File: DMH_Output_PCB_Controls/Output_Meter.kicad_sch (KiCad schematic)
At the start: 63 parts, among them Q1 BC558, Q2 BC558, U1 TL072, U2 LM339, U3 LM339, U4 LM339, U5 LM339, U6 LM339

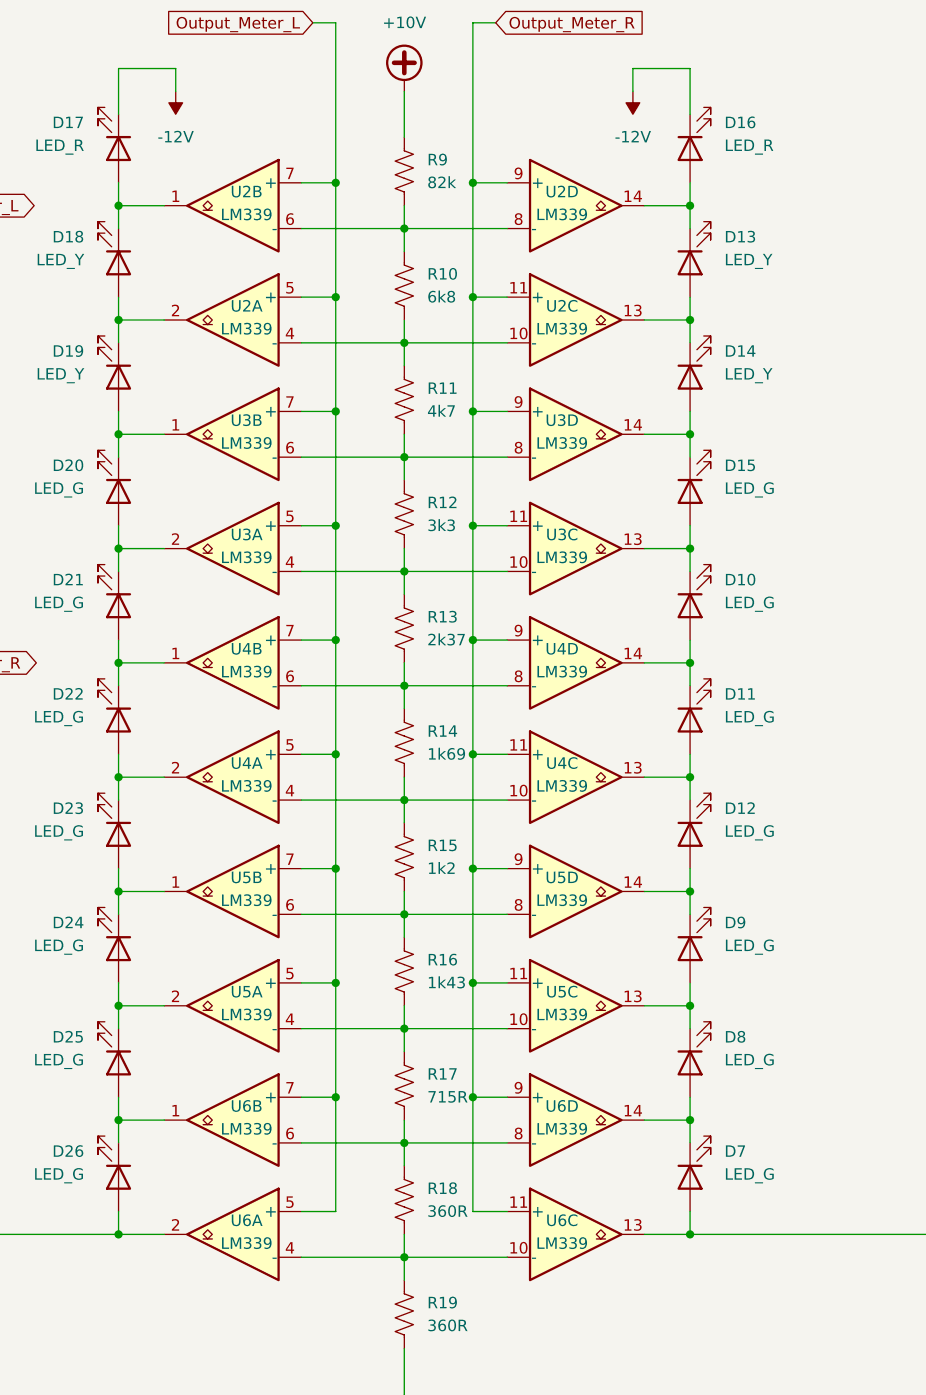
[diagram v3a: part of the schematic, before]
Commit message: Re-arranged LM339 connections
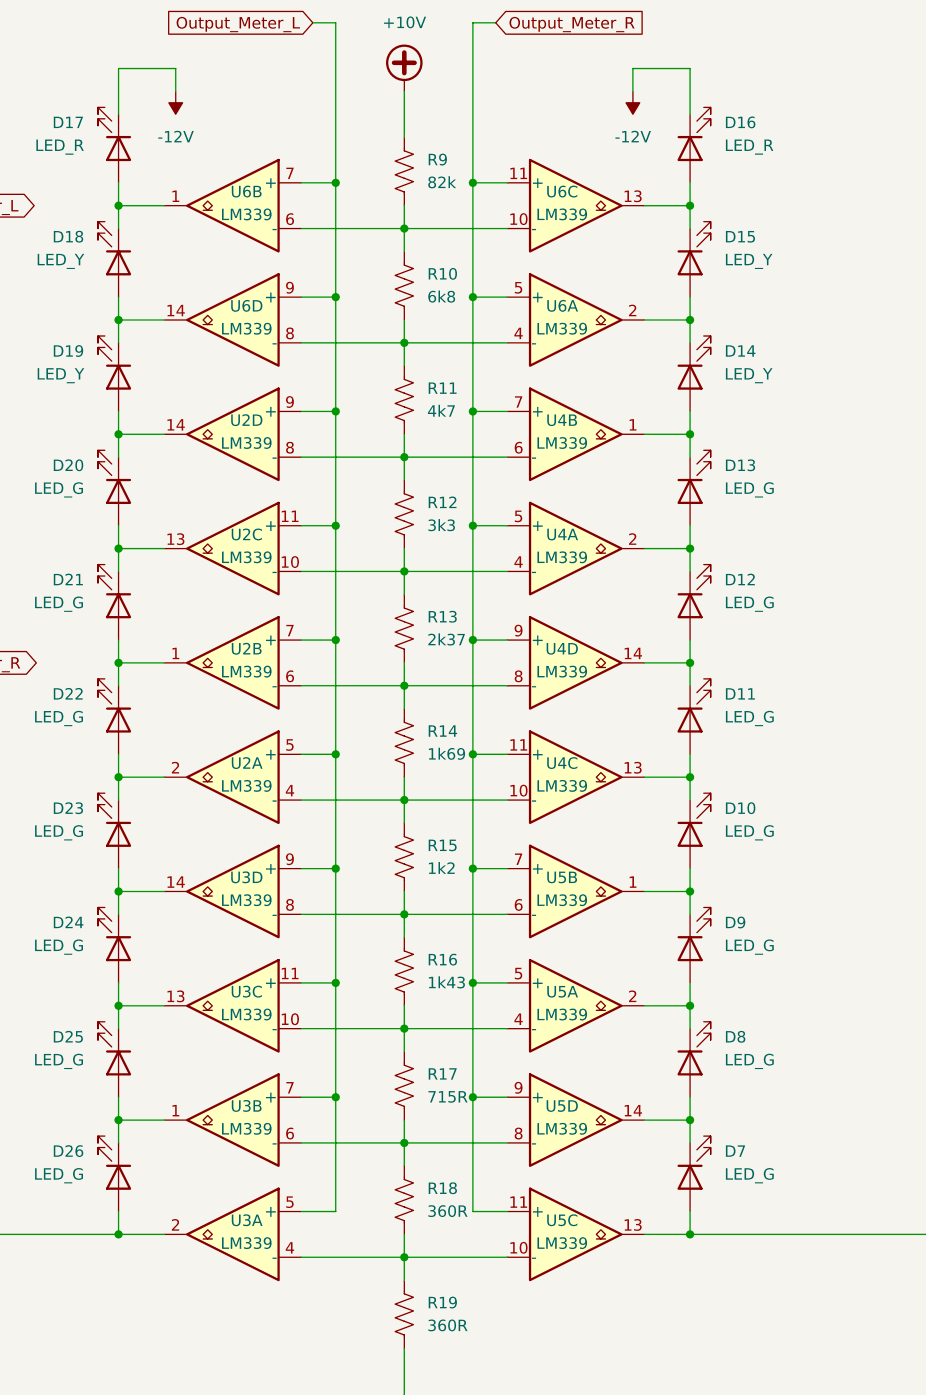
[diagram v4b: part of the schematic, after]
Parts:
- renumbered D12 to D10, D10 to D12, D15 to D13, D13 to D15, U4 to U2, U3 to U2, U6 to U3, U5 to U3, U3 to U4, U6 to U5, U2 to U6
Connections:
- net Output_Meter_L: now also U2.11 (+), U2.9 (+), U3.11 (+), U3.9 (+), U6.9 (+); no longer U2.5 (+), U2.7 (+), U3.5 (+), U3.7 (+), U6.5 (+)
- net Output_Meter_R: now also U4.5 (+), U4.7 (+), U5.5 (+), U5.7 (+), U6.11 (+), U6.5 (+); no longer U4.11 (+), U4.9 (+), U5.11 (+), U5.9 (+), U6.11 (+), U6.9 (+)
- net at R12.1, R13.2: now also U2.10 (-), U4.4 (-); no longer U2.4 (-), U4.10 (-)
- net at D12.1 (K), D13.2 (A): now also U4.2; no longer U4.13
- net at D23.2 (A), D24.1 (K): now also U3.14; no longer U3.1
- net at D24.2 (A), D25.1 (K): now also U3.13; no longer U3.2
- net at D19.2 (A), D20.1 (K): now also U2.14; no longer U2.1
- net at D20.2 (A), D21.1 (K): now also U2.13; no longer U2.2
- net at R11.1, R12.2: now also U2.8 (-), U4.6 (-); no longer U2.6 (-), U4.8 (-)
- net at R10.1, R11.2: now also U6.4 (-), U6.8 (-); no longer U6.10 (-), U6.4 (-)
- net at D8.1 (K), D9.2 (A): now also U5.2; no longer U5.13
- net at D13.1 (K), D14.2 (A): now also U4.1; no longer U4.14
- net at R16.1, R17.2: now also U3.10 (-), U5.4 (-); no longer U3.4 (-), U5.10 (-)
- net at R15.1, R16.2: now also U3.8 (-), U5.6 (-); no longer U3.6 (-), U5.8 (-)
- net at D15.1 (K), D16.2 (A): now also U6.13; no longer U6.14
- net at R10.2, R9.1, U6.6 (-): now also U6.10 (-); no longer U6.8 (-)
- net at D18.2 (A), D19.1 (K): now also U6.14; no longer U6.2
- net at D10.2 (A), D9.1 (K): now also U5.1; no longer U5.14
- net at D14.1 (K), D15.2 (A): now also U6.2; no longer U6.13
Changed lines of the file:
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@@
 		(on_board yes)
 		(dnp no)
-		(property "Reference" "U4"
+		(property "Reference" "U2"
 			(at 153.924 87.376 0)
 			(effects
@@
 			(project "DMH_Output_PCB_1"
 				(path "/58f4306d-5387-4983-bb08-41a2313fd315/91d96a83-7777-458d-a0c8-9961efcb16a5"
-					(reference "U4")
+					(reference "U2")
 					(unit 2)
 				)
@@
 		(lib_id "Comparator:LM339")
 		(at 190.5 76.2 0)
-		(unit 3)
+		(unit 1)
 		(exclude_from_sim no)
 		(in_bom yes)
 		(on_board yes)
 		(dnp no)
-		(property "Reference" "U3"
+		(property "Reference" "U4"
 			(at 188.976 74.676 0)
 			(effects
@@
 			(project "DMH_Output_PCB_1"
 				(path "/58f4306d-5387-4983-bb08-41a2313fd315/91d96a83-7777-458d-a0c8-9961efcb16a5"
-					(reference "U3")
-					(unit 3)
+					(reference "U4")
+					(unit 1)
 				)
 			)
@@
 		(on_board yes)
 		(dnp no)
-		(property "Reference" "U4"
+		(property "Reference" "U2"
 			(at 153.924 100.076 0)
 			(effects
@@
 			(project "DMH_Output_PCB_1"
 				(path "/58f4306d-5387-4983-bb08-41a2313fd315/91d96a83-7777-458d-a0c8-9961efcb16a5"
-					(reference "U4")
+					(reference "U2")
 					(unit 1)
 				)
@@
 		(on_board yes)
 		(dnp no)
-		(property "Reference" "U6"
+		(property "Reference" "U5"
 			(at 188.976 138.176 0)
 			(effects
@@
 			(project "DMH_Output_PCB_1"
 				(path "/58f4306d-5387-4983-bb08-41a2313fd315/91d96a83-7777-458d-a0c8-9961efcb16a5"
-					(reference "U6")
+					(reference "U5")
 					(unit 4)
 				)
@@
 		(dnp no)
 		(fields_autoplaced yes)
-		(property "Reference" "D15"
+		(property "Reference" "D13"
 			(at 207.01 66.9924 90)
 			(effects
@@
 			(project "DMH_Output_PCB_1"
 				(path "/58f4306d-5387-4983-bb08-41a2313fd315/91d96a83-7777-458d-a0c8-9961efcb16a5"
-					(reference "D15")
+					(reference "D13")
 					(unit 1)
 				)
@@
 		(on_board yes)
 		(dnp no)
-		(property "Reference" "U6"
+		(property "Reference" "U3"
 			(at 153.924 138.176 0)
 			(effects
@@
 			(project "DMH_Output_PCB_1"
 				(path "/58f4306d-5387-4983-bb08-41a2313fd315/91d96a83-7777-458d-a0c8-9961efcb16a5"
-					(reference "U6")
+					(reference "U3")
 					(unit 2)
 				)
@@
 		(on_board yes)
 		(dnp no)
-		(property "Reference" "U6"
+		(property "Reference" "U3"
 			(at 153.924 150.876 0)
 			(effects
@@
 			(project "DMH_Output_PCB_1"
 				(path "/58f4306d-5387-4983-bb08-41a2313fd315/91d96a83-7777-458d-a0c8-9961efcb16a5"
-					(reference "U6")
+					(reference "U3")
 					(unit 1)
 				)
@@
 		(lib_id "Comparator:LM339")
 		(at 190.5 38.1 0)
-		(unit 4)
+		(unit 3)
 		(exclude_from_sim no)
 		(in_bom yes)
 		(on_board yes)
 		(dnp no)
-		(property "Reference" "U2"
+		(property "Reference" "U6"
 			(at 188.976 36.576 0)
 			(effects
@@
 			(project "DMH_Output_PCB_1"
 				(path "/58f4306d-5387-4983-bb08-41a2313fd315/91d96a83-7777-458d-a0c8-9961efcb16a5"
-					(reference "U2")
-					(unit 4)
+					(reference "U6")
+					(unit 3)
 				)
 			)
@@
 		(at 152.4 76.2 0)
 		(mirror y)
-		(unit 1)
+		(unit 3)
 		(exclude_from_sim no)
 		(in_bom yes)
 		(on_board yes)
 		(dnp no)
-		(property "Reference" "U3"
+		(property "Reference" "U2"
 			(at 153.924 74.676 0)
 			(effects
@@
 			(project "DMH_Output_PCB_1"
 				(path "/58f4306d-5387-4983-bb08-41a2313fd315/91d96a83-7777-458d-a0c8-9961efcb16a5"
-					(reference "U3")
-					(unit 1)
+					(reference "U2")
+					(unit 3)
 				)
 			)
@@
 		(at 152.4 63.5 0)
 		(mirror y)
-		(unit 2)
+		(unit 4)
 		(exclude_from_sim no)
 		(in_bom yes)
 		(on_board yes)
 		(dnp no)
-		(property "Reference" "U3"
+		(property "Reference" "U2"
 			(at 153.924 61.976 0)
 			(effects
@@
 			(project "DMH_Output_PCB_1"
 				(path "/58f4306d-5387-4983-bb08-41a2313fd315/91d96a83-7777-458d-a0c8-9961efcb16a5"
-					(reference "U3")
-					(unit 2)
+					(reference "U2")
+					(unit 4)
 				)
 			)
@@
 		(dnp no)
 		(fields_autoplaced yes)
-		(property "Reference" "D12"
+		(property "Reference" "D10"
 			(at 207.01 105.0924 90)
 			(effects
@@
 			(project "DMH_Output_PCB_1"
 				(path "/58f4306d-5387-4983-bb08-41a2313fd315/91d96a83-7777-458d-a0c8-9961efcb16a5"
-					(reference "D12")
+					(reference "D10")
 					(unit 1)
 				)
@@
 		(dnp no)
 		(fields_autoplaced yes)
-		(property "Reference" "D10"
+		(property "Reference" "D12"
 			(at 207.01 79.6924 90)
 			(effects
@@
 			(project "DMH_Output_PCB_1"
 				(path "/58f4306d-5387-4983-bb08-41a2313fd315/91d96a83-7777-458d-a0c8-9961efcb16a5"
-					(reference "D10")
+					(reference "D12")
 					(unit 1)
 				)
@@
 		(at 152.4 50.8 0)
 		(mirror y)
-		(unit 1)
+		(unit 4)
 		(exclude_from_sim no)
 		(in_bom yes)
 		(on_board yes)
 		(dnp no)
-		(property "Reference" "U2"
+		(property "Reference" "U6"
 			(at 153.924 49.276 0)
 			(effects
@@
 			(project "DMH_Output_PCB_1"
 				(path "/58f4306d-5387-4983-bb08-41a2313fd315/91d96a83-7777-458d-a0c8-9961efcb16a5"
-					(reference "U2")
-					(unit 1)
+					(reference "U6")
+					(unit 4)
 				)
 			)
@@
 		(lib_id "Comparator:LM339")
 		(at 190.5 63.5 0)
-		(unit 4)
+		(unit 2)
 		(exclude_from_sim no)
 		(in_bom yes)
 		(on_board yes)
 		(dnp no)
-		(property "Reference" "U3"
+		(property "Reference" "U4"
 			(at 188.976 61.976 0)
 			(effects
@@
 			(project "DMH_Output_PCB_1"
 				(path "/58f4306d-5387-4983-bb08-41a2313fd315/91d96a83-7777-458d-a0c8-9961efcb16a5"
-					(reference "U3")
-					(unit 4)
+					(reference "U4")
+					(unit 2)
 				)
 			)
@@
 		(at 152.4 114.3 0)
 		(mirror y)
-		(unit 2)
+		(unit 4)
 		(exclude_from_sim no)
 		(in_bom yes)
 		(on_board yes)
 		(dnp no)
-		(property "Reference" "U5"
+		(property "Reference" "U3"
 			(at 153.924 112.776 0)
 			(effects
@@
 			(project "DMH_Output_PCB_1"
 				(path "/58f4306d-5387-4983-bb08-41a2313fd315/91d96a83-7777-458d-a0c8-9961efcb16a5"
-					(reference "U5")
-					(unit 2)
+					(reference "U3")
+					(unit 4)
 				)
 			)
@@
 		(dnp no)
 		(fields_autoplaced yes)
-		(property "Reference" "D13"
+		(property "Reference" "D15"
 			(at 207.01 41.5924 90)
 			(effects
@@
 			(project "DMH_Output_PCB_1"
 				(path "/58f4306d-5387-4983-bb08-41a2313fd315/91d96a83-7777-458d-a0c8-9961efcb16a5"
-					(reference "D13")
+					(reference "D15")
 					(unit 1)
 				)
@@
 		(lib_id "Comparator:LM339")
 		(at 190.5 127 0)
-		(unit 3)
+		(unit 1)
 		(exclude_from_sim no)
 		(in_bom yes)
@@
 				(path "/58f4306d-5387-4983-bb08-41a2313fd315/91d96a83-7777-458d-a0c8-9961efcb16a5"
 					(reference "U5")
-					(unit 3)
+					(unit 1)
 				)
 			)
@@
 		(on_board yes)
 		(dnp no)
-		(property "Reference" "U6"
+		(property "Reference" "U5"
 			(at 188.976 150.876 0)
 			(effects
@@
 			(project "DMH_Output_PCB_1"
 				(path "/58f4306d-5387-4983-bb08-41a2313fd315/91d96a83-7777-458d-a0c8-9961efcb16a5"
-					(reference "U6")
+					(reference "U5")
 					(unit 3)
 				)
@@
 		(on_board yes)
 		(dnp no)
-		(property "Reference" "U2"
+		(property "Reference" "U6"
 			(at 153.924 36.576 0)
 			(effects
@@
 			)
 		)
+		(property "Function" ""
+			(at 152.4 38.1 0)
+			(effects
+				(font
+					(size 1.27 1.27)
+				)
+			)
+		)
 		(pin "7"
 		)
@@
 			(project "DMH_Output_PCB_1"
 				(path "/58f4306d-5387-4983-bb08-41a2313fd315/91d96a83-7777-458d-a0c8-9961efcb16a5"
-					(reference "U2")
+					(reference "U6")
 					(unit 2)
 				)
@@
 		(lib_id "Comparator:LM339")
 		(at 190.5 114.3 0)
-		(unit 4)
+		(unit 2)
 		(exclude_from_sim no)
 		(in_bom yes)
@@
 				(path "/58f4306d-5387-4983-bb08-41a2313fd315/91d96a83-7777-458d-a0c8-9961efcb16a5"
 					(reference "U5")
-					(unit 4)
+					(unit 2)
 				)
 			)
@@
 		(at 152.4 127 0)
 		(mirror y)
-		(unit 1)
+		(unit 3)
 		(exclude_from_sim no)
 		(in_bom yes)
 		(on_board yes)
 		(dnp no)
-		(property "Reference" "U5"
+		(property "Reference" "U3"
 			(at 153.924 125.476 0)
 			(effects
@@
 			(project "DMH_Output_PCB_1"
 				(path "/58f4306d-5387-4983-bb08-41a2313fd315/91d96a83-7777-458d-a0c8-9961efcb16a5"
-					(reference "U5")
-					(unit 1)
+					(reference "U3")
+					(unit 3)
 				)
 			)
@@
 		(lib_id "Comparator:LM339")
 		(at 190.5 50.8 0)
-		(unit 3)
+		(unit 1)
 		(exclude_from_sim no)
 		(in_bom yes)
 		(on_board yes)
 		(dnp no)
-		(property "Reference" "U2"
+		(property "Reference" "U6"
 			(at 188.976 49.276 0)
 			(effects
@@
 			(project "DMH_Output_PCB_1"
 				(path "/58f4306d-5387-4983-bb08-41a2313fd315/91d96a83-7777-458d-a0c8-9961efcb16a5"
-					(reference "U2")
-					(unit 3)
+					(reference "U6")
+					(unit 1)
 				)
 			)
